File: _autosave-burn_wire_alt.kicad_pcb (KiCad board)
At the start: 2 copper layers, 30.2 x 26 mm, 21 parts, among them J1 Conn_01x02_Pin, J1 TestPoint_THTPad_1.0x1.0mm_Dr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, J2 Conn_01x02_Pin, U1 ADP2303ARDZ

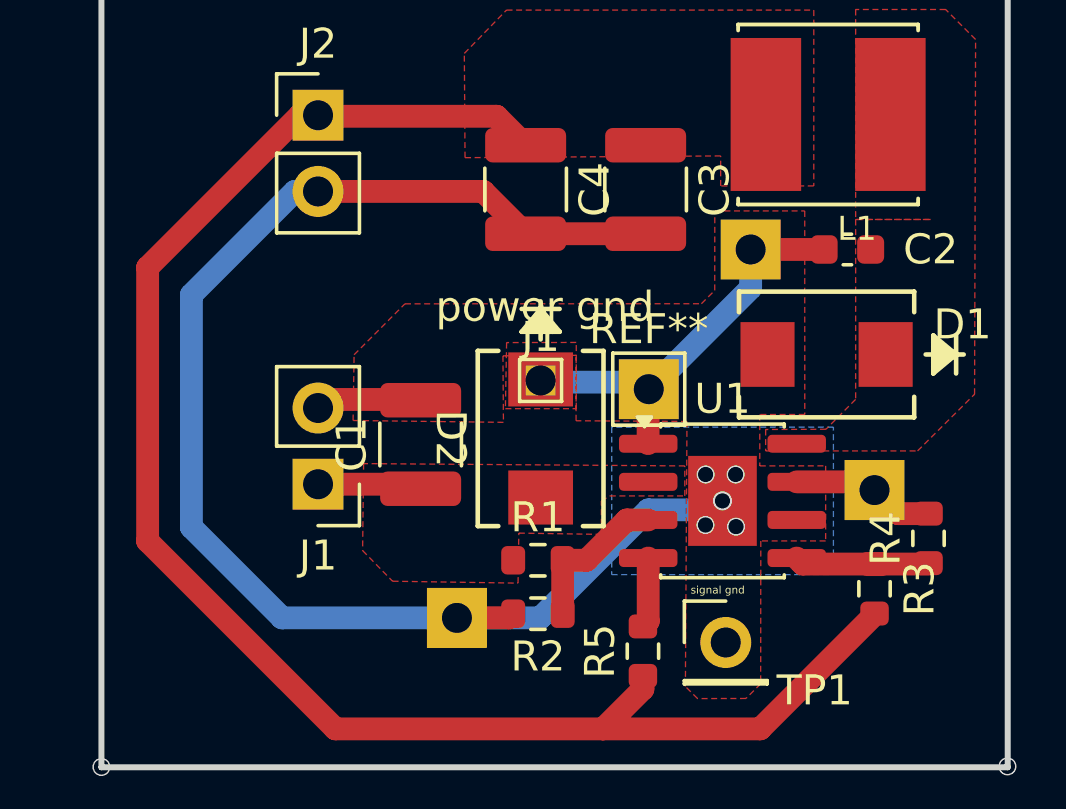
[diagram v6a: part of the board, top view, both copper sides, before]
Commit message: cout connected to noisy gnd
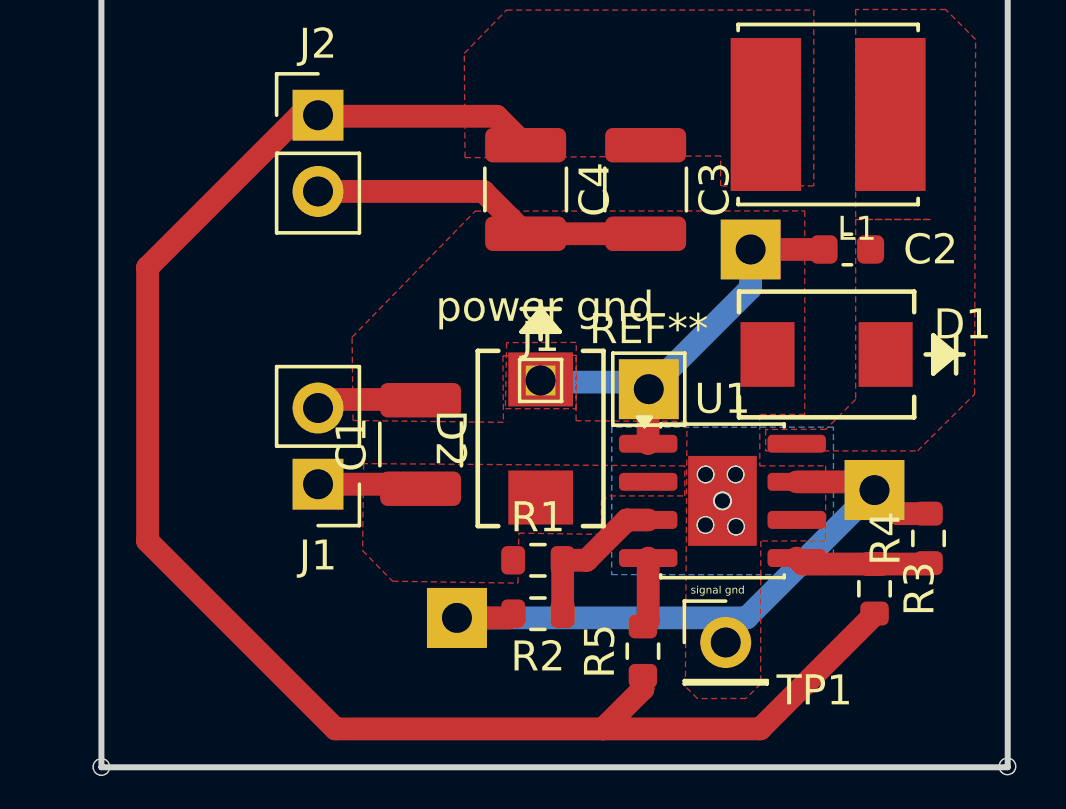
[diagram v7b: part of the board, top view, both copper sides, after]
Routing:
- net GND: track 55.8 -> 37.5 mm
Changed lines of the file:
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@@
 	)
 	(segment
-		(start 152.86 87.51)
-		(end 152.86 95.26)
-		(width 0.762)
-		(layer "B.Cu")
-		(net "GND")
-	)
-	(segment
-		(start 164.49 98.28)
-		(end 168.09 94.68)
-		(width 0.762)
-		(layer "B.Cu")
-		(net "GND")
-	)
-	(segment
-		(start 170.262221 94.68)
-		(end 170.561611 94.38061)
-		(width 0.762)
-		(layer "B.Cu")
-		(net "GND")
-	)
-	(segment
-		(start 168.09 94.68)
-		(end 170.262221 94.68)
-		(width 0.762)
-		(layer "B.Cu")
-		(net "GND")
-	)
-	(segment
-		(start 152.86 95.26)
-		(end 155.88 98.28)
-		(width 0.762)
-		(layer "B.Cu")
-		(net "GND")
-	)
-	(segment
-		(start 155.88 98.28)
-		(end 161.71 98.28)
-		(width 0.762)
-		(layer "B.Cu")
-		(net "GND")
-	)
-	(segment
-		(start 156.305 84.065)
-		(end 152.86 87.51)
+		(start 171.37 98.28)
+		(end 175.63 94.02)
 		(width 0.762)
 		(layer "B.Cu")
@@
 	(segment
 		(start 161.71 98.28)
-		(end 164.49 98.28)
-		(width 0.762)
-		(layer "B.Cu")
-		(net "GND")
-	)
-	(segment
-		(start 157.08 84.065)
-		(end 156.305 84.065)
+		(end 171.37 98.28)
 		(width 0.762)
 		(layer "B.Cu")
@@
 		(polygon
 			(pts
-				(xy 158.281968 89.508912) (xy 159.978074 87.811601) (xy 169.859993 87.808537) (xy 170.303757 87.365234)
-				(xy 170.305137 84.71487) (xy 173.303604 84.71487) (xy 173.304518 91.5) (xy 171.80416 91.500852)
+				(xy 158.215307 88.923445) (xy 162.32 84.72) (xy 173.303604 84.71487) (xy 173.304518 91.5) (xy 171.80416 91.500852)
 				(xy 171.805265 93.213933) (xy 174 93.212518) (xy 174 95.71487) (xy 171.838896 95.715834) (xy 171.835039 100.477078)
 				(xy 171.345326 100.965999) (xy 169.731306 100.970391) (xy 169.325285 100.566216) (xy 169.377999 91.731751)

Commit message: board 2 for 6/3
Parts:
- removed the J1 at (164.5, 90.4)
- removed TP1: PinHeader_1x01_P2.54mm_Vertical, Connector_PinHeader_2.54mm:PinHeader_1x01_P2.54mm_Vertical
- added ?: , , F.Cu at (164.5, 90.4)
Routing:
- net /Vout: track 55.0 -> 55.9 mm
- net GND: track 37.5 -> 38.1 mm
